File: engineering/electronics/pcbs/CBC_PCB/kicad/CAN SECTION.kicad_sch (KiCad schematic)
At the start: 44 parts, among them U14 TJA1049T/3J, U26 ADM3053BRWZ-REEL7, X1 16MHz, X2 16MHz

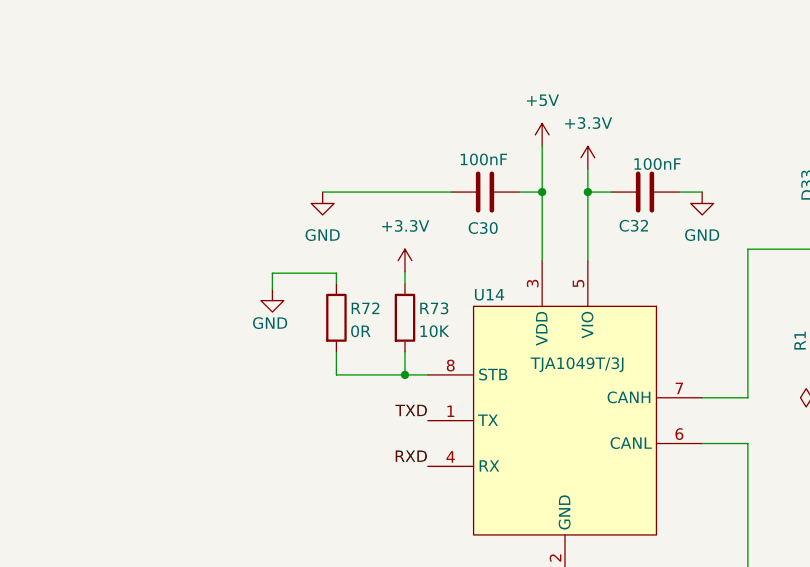
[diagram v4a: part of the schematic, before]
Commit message: sch: fix simple CBC ERC issues
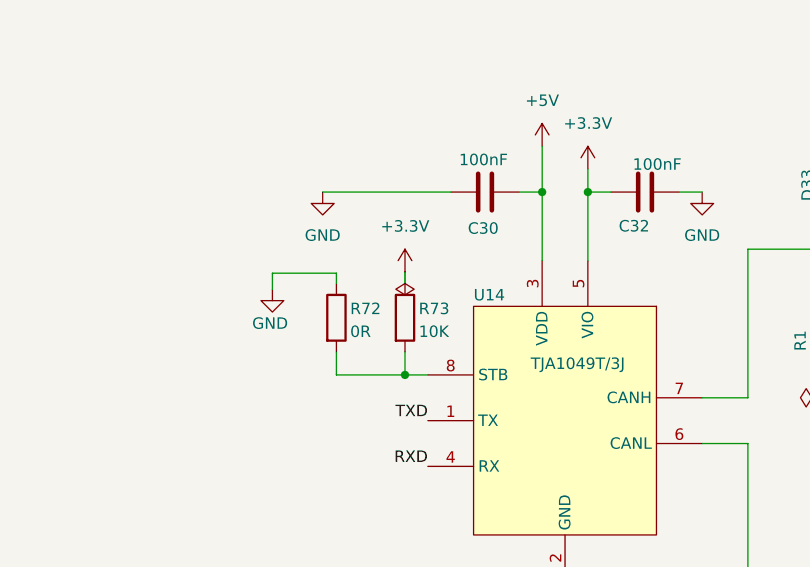
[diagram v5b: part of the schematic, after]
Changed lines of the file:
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@@
+	)
+	(symbol
+		(lib_id "power:PWR_FLAG")
+		(at 179.832 49.784 180)
+		(unit 1)
+		(body_style 1)
+		(exclude_from_sim no)
+		(in_bom yes)
+		(on_board yes)
+		(in_pos_files yes)
+		(dnp no)
+		(property "Reference" "#FLG086"
+			(at 179.832 51.054 0)
+			(hide yes)
+			(show_name no)
+			(do_not_autoplace no)
+			(effects
+				(font
+					(size 1.27 1.27)
+				)
+			)
+		)
+		(property "Value" "PWR_FLAG"
+			(at 179.832 54.864 0)
+			(hide yes)
+			(show_name no)
+			(do_not_autoplace no)
+			(effects
+				(font
+					(size 1.27 1.27)
+				)
+			)
+		)
+		(property "Footprint" ""
+			(at 179.832 49.784 0)
+			(hide yes)
+			(show_name no)
+			(do_not_autoplace no)
+			(effects
+				(font
+					(size 1.27 1.27)
+				)
+			)
+		)
+		(property "Datasheet" ""
+			(at 179.832 49.784 0)
+			(hide yes)
+			(show_name no)
+			(do_not_autoplace no)
+			(effects
+				(font
+					(size 1.27 1.27)
+				)
+			)
+		)
+		(property "Description" "Special symbol for telling ERC where power comes from"
+			(at 179.832 49.784 0)
+			(hide yes)
+			(show_name no)
+			(do_not_autoplace no)
+			(effects
+				(font
+					(size 1.27 1.27)
+				)
+			)
+		)
+		(pin "1"
+		)
+		(instances
+			(project "CBC_PCB"
+				(path "/d195d1ee-585b-4211-912f-f5dd5687bc63/b93821f7-9505-4d21-a91e-b5687eb30748"
+					(reference "#FLG086")
+					(unit 1)
+				)
+			)
+		)
 	)
 	(symbol
